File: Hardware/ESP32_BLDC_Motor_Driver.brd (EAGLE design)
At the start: 86.4 x 57.1 mm, 112 parts, among them J2 0532610371, J3 POWER_JACKPOWER_JACK_SLOT, J6 0.1in header, J7 QWIIC_RIGHT_ANGLE, Q1 20V/4.2A/52mΩ/1.4W, U1 TMC6300, U2 OPA344, U3 ESP-WROOM-3232D-NARROW, U4 CH340C, U5 ESD Diode, U6 AP63357, U7 AP2202-ADJ, U8 TMAG5273

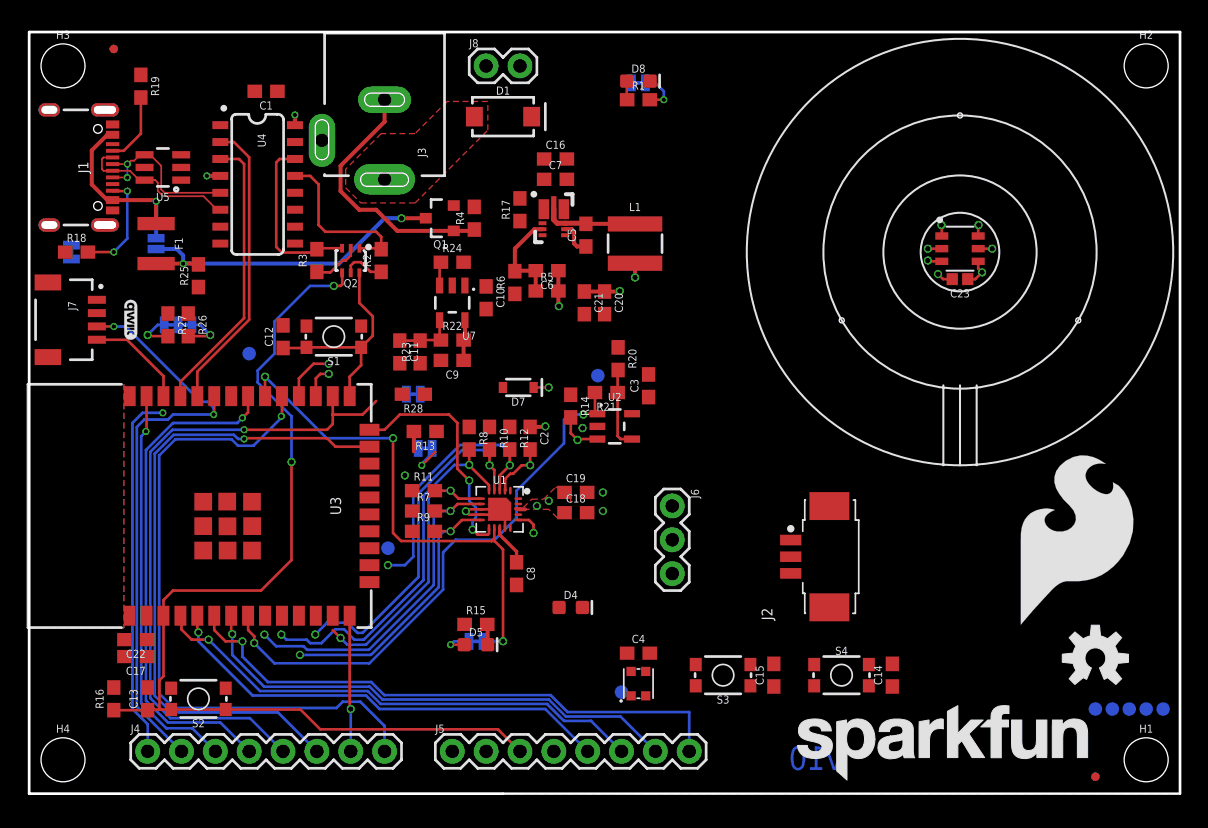
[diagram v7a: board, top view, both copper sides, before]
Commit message: Layout Updates
Completed all air wires and most design rule errors - still a few to go. Layout primarily solidified. logos, name, and labels added to board.
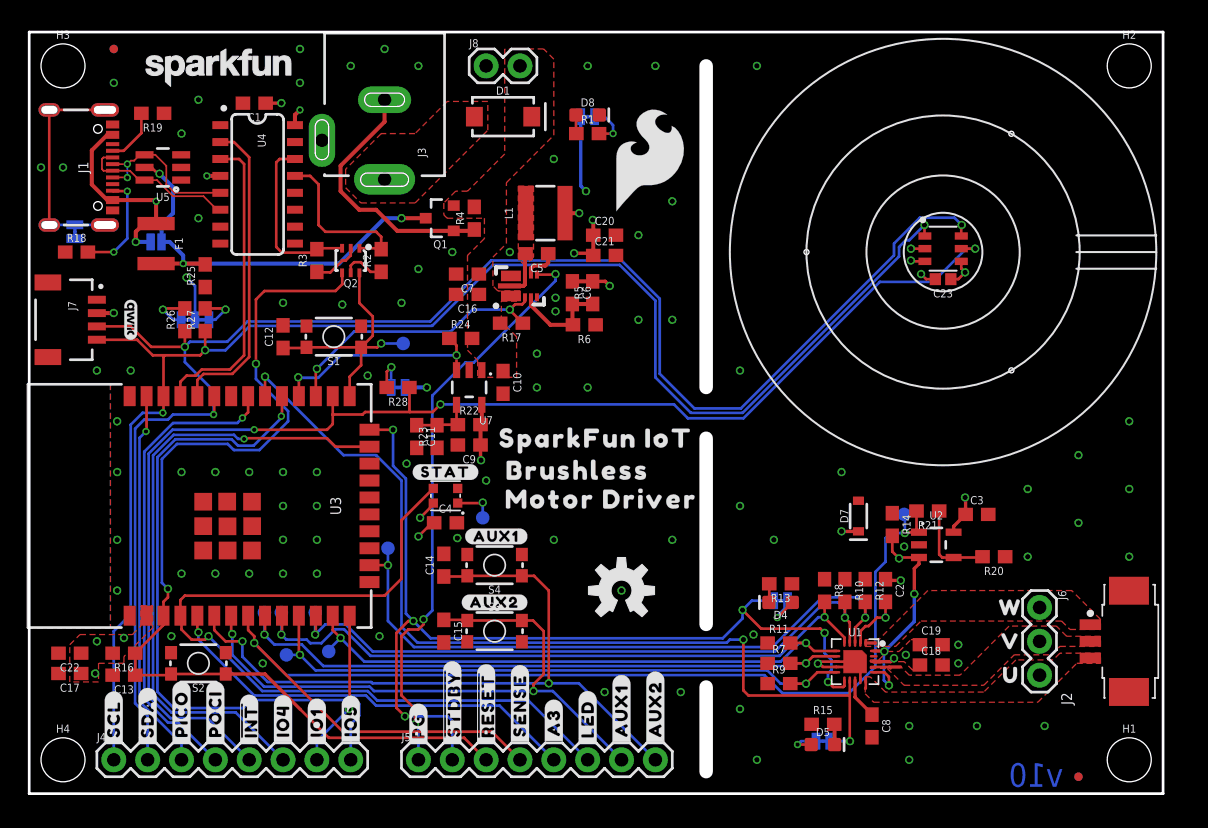
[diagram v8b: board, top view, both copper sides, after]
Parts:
- removed D2: WS2812_2020, SparkFun-LED:WS2812-2020
- added STAT: WS2812_2020, SparkFun-LED:WS2812-2020
- added U$10: (no value), output:#IO4#630063003461
- added U$11: (no value), output:#IO1#630063003461
- added U$12: (no value), output:#IO5#630063003461
- added U$13: (no value), output:##INT#630063003461
- added U$14: (no value), output:#POCI#630063003462
- added U$15: (no value), output:#PICO#630063003463
- added U$16: (no value), output:#SDA#630063003464
- added U$17: (no value), output:#SCL#630063003465
- added U$18: (no value), output:#AUX2#630063003471
- added U$19: (no value), output:#BYP#630063003471
- added U$20: (no value), output:#D#630063003474
- added U$21: (no value), output:#A3#630063003466
- added U$22: (no value), output:#AUX1#630063003471
- added U$23: (no value), output:#I2C#630063003467
- added U$24: (no value), output:#SHLD#630063003467
- added U$25: (no value), output:##INT#630063003473
- added U$26: (no value), output:#PWR#630063003472
- added U$27: (no value), output:#STAT#630063003470
- added U$28: (no value), output:#S#630063003475
- added U$29: (no value), output:#_SCL#630063003479
- added U$3: (no value), output:#PG#630063003456
- added U$30: (no value), output:#_SDA#630063003480
- added U$31: (no value), output:#_PICO#630063003481
- added U$32: (no value), output:#_POCI#630063003482
- added U$33: (no value), output:#_#INT#630063003483
- added U$34: (no value), output:#_IO4#630063003484
- added U$35: (no value), output:#_IO1#630063003484
- added U$36: (no value), output:#_IO2#630063003484
- added U$37: (no value), output:#_PG#630063003484
- added U$38: (no value), output:#_#STDBY#630063003485
- added U$39: (no value), output:#_#RESET#630063003486
- added U$4: (no value), output:##STDBY#630063003457
- added U$40: (no value), output:#_SENSE#630063003487
- added U$41: (no value), output:#_A3#630063003488
- added U$42: (no value), output:#_LED#630063003488
- added U$43: (no value), output:#_AUX1#630063003489
- added U$44: (no value), output:#_AUX2#630063003489
- added U$45: (no value), SparkFun-Aesthetics:SFE_LOGO_NAME_FLAME_.2
- added U$46: (no value), output:SPARKFUN_IOT630063003504
- added U$47: (no value), output:BRUSHLESS630063003505
- added U$48: (no value), output:MOTOR_DRIVER630063003506
- added U$49: (no value), output:U630063003494
- added U$5: (no value), output:##RESET#630063003458
- added U$50: (no value), output:V630063003496
- added U$51: (no value), output:W630063003497
- added U$6: (no value), output:#SENSE#630063003459
- added U$7: (no value), output:#LED#630063003460
- added U$8: (no value), output:#AUX1#630063003461
- added U$9: (no value), output:#AUX2#630063003461
- J1: value (none) -> USB-C Connector
- J4: value (none) -> Breadboard Connector
- J5: value (none) -> Breadboard Headers
- J8: value (none) -> Breakout Header
- LOGO3: value SFE_LOGO_FLAME.5_INCH -> SFE_LOGO_FLAME.3_INCH; device SparkFun-Aesthetics:SFE_LOGO_FLAME_.5 -> SparkFun-Aesthetics:SFE_LOGO_FLAME_.3
- LOGO5: value SFE_LOGO_NAME.2_INCH -> SFE_LOGO_NAME.1_INCH; device SparkFun-Aesthetics:SFE_LOGO_NAME_.2 -> SparkFun-Aesthetics:SFE_LOGO_NAME_.1
- Q2: value (none) -> NPN Transistors
- moved LOGO5 74.3 mm to (14.2, 54.5)
- moved TP6 63.4 mm to (19.3, 10.4)
- moved TP8 62.8 mm to (17.7, 13.6)
- moved TP7 62.8 mm to (18.9, 13.6)
- moved TP5 62.8 mm to (21.5, 13.6)
- moved TP4 62.8 mm to (22.5, 10.7)
- moved LOGO3 42.9 mm to (46.6, 47.5)
- moved LOGO2 35.9 mm to (44.5, 15.2)
- moved C14 34.7 mm to (31.1, 17.1)
- moved R20 31.9 mm to (72.4, 17.8), turned to 180 degrees
- moved C18 29.0 mm to (67.7, 9.65)
- moved C19 29.0 mm to (67.7, 11.2)
- moved C2 29.0 mm to (64.3, 15.2)
- moved C8 29.0 mm to (63.2, 5.08)
- moved R10 29.0 mm to (61.2, 15.2)
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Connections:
- net 3.3V_LDO: now also STAT.VCC; no longer D2.VCC
- net ESP_36/LED: now also STAT.DI; no longer D2.DI
- net GND: now also STAT.GND; no longer D2.GND
- net TP2: now also STAT.DO; no longer D2.DO
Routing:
- net ESP_22/TP_SCL: track 36.2 -> 114.7 mm, vias 2 -> 3
- net ESP_21/TP_SDA: track 45.9 -> 123.7 mm
- net ESP_0/!STDBY: track 17.9 -> 73.4 mm, vias 2 -> 6
- net ESP_4/!INT: track 51.5 -> 101.7 mm, vias 2 -> 3
- net ESP_32/CURR_SENSE: track 41.9 -> 90.5 mm
- net 3.3V_PG: track 0.00 -> 44.0 mm, vias 0 -> 3
- net ESP_18/DIAG: track 38.6 -> 70.2 mm
- net ESP_13/UH: track 20.3 -> 49.6 mm
- net ESP_26/VL: track 21.3 -> 46.7 mm
- net ESP_36/LED: track 37.9 -> 62.1 mm
- net ESP_33/WL: track 25.5 -> 48.5 mm
- net ESP_27/VH: track 27.3 -> 49.6 mm
- net ESP_25/WH: track 28.0 -> 50.3 mm
- net ESP_14/UL: track 21.5 -> 43.2 mm
- net ESP_16/EN_MOTOR_PWR: track 2.44 -> 21.5 mm, vias 1 -> 2
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- added copper zone on layer 1, net 3.3V_LDO
- added copper zone on layer 1, net SW
- added copper zone on layer 1, net U
- added copper zone on layer 1, net V
- added copper zone on layer 1, net VIN
- added copper zone on layer 1, net W
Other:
- board size 86.4 x 57.1 mm -> 85.1 x 57.1 mm
